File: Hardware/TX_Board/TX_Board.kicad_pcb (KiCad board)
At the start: 2 copper layers, 153 x 131.5 mm, 218 parts, among them IC1 QPA9122TR7, IC10 QPA9122TR7, IC11 QPA9122TR7, IC12 LT3041ADE#PBF, IC13 LT3099ADE#PBF, IC14 ADPL40502AUJZ-1.5-R7, IC2 MAPS-010164-TR0500, IC3 MAPS-010164-TR0500, IC4 QPA9122TR7, IC5 GP2Y1+, IC6 GP2Y1+, IC7 GP2Y1+, IC8 MAPS-010164-TR0500, IC9 MAPS-010164-TR0500, J1 Conn_Coaxial, J10 Conn_01x01_Pin, J11 Conn_Coaxial, J12 Conn_02x04_Odd_Even, J13 MM8030-2610RJ3, J14 MM8030-2610RJ3, J15 MM8030-2610RJ3, J16 MM8030-2610RJ3, J17 MM8030-2610RJ3, J18 MM8030-2610RJ3, J19 MM8030-2610RJ3, J2 Conn_Coaxial, J20 MM8030-2610RJ3, J21 MM8030-2610RJ3, J22 MM8030-2610RJ3, J23 MM8030-2610RJ3, J24 MM8030-2610RJ3, J3 Conn_Coaxial, J4 Conn_Coaxial, J5 Conn_02x08_Odd_Even, J6 Conn_01x03_Socket, J7 Conn_01x01_Pin, J8 Conn_01x01_Pin, J9 Conn_01x01_Pin, U1 SN74HCT138NSR, U2 LDO40LPU50RY, U3 ADP7182AUJZ-5.0

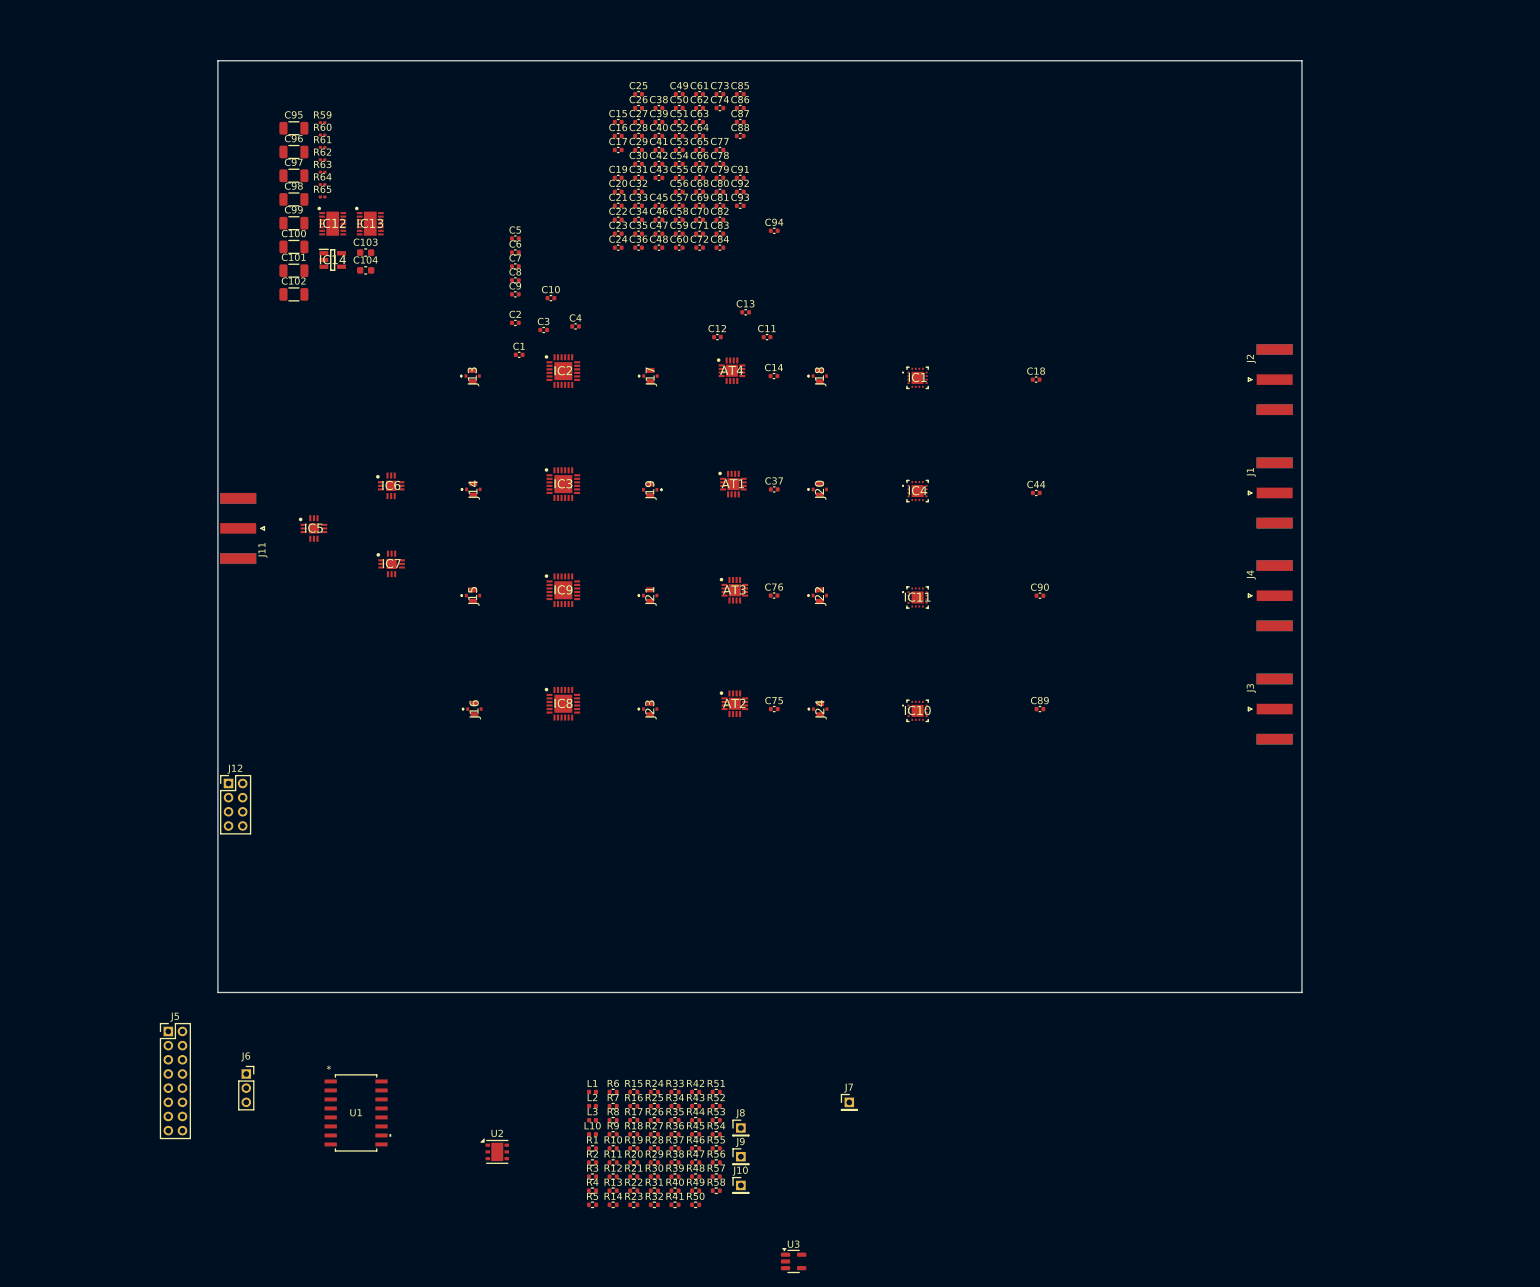
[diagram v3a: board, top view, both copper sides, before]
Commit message: updated schematics
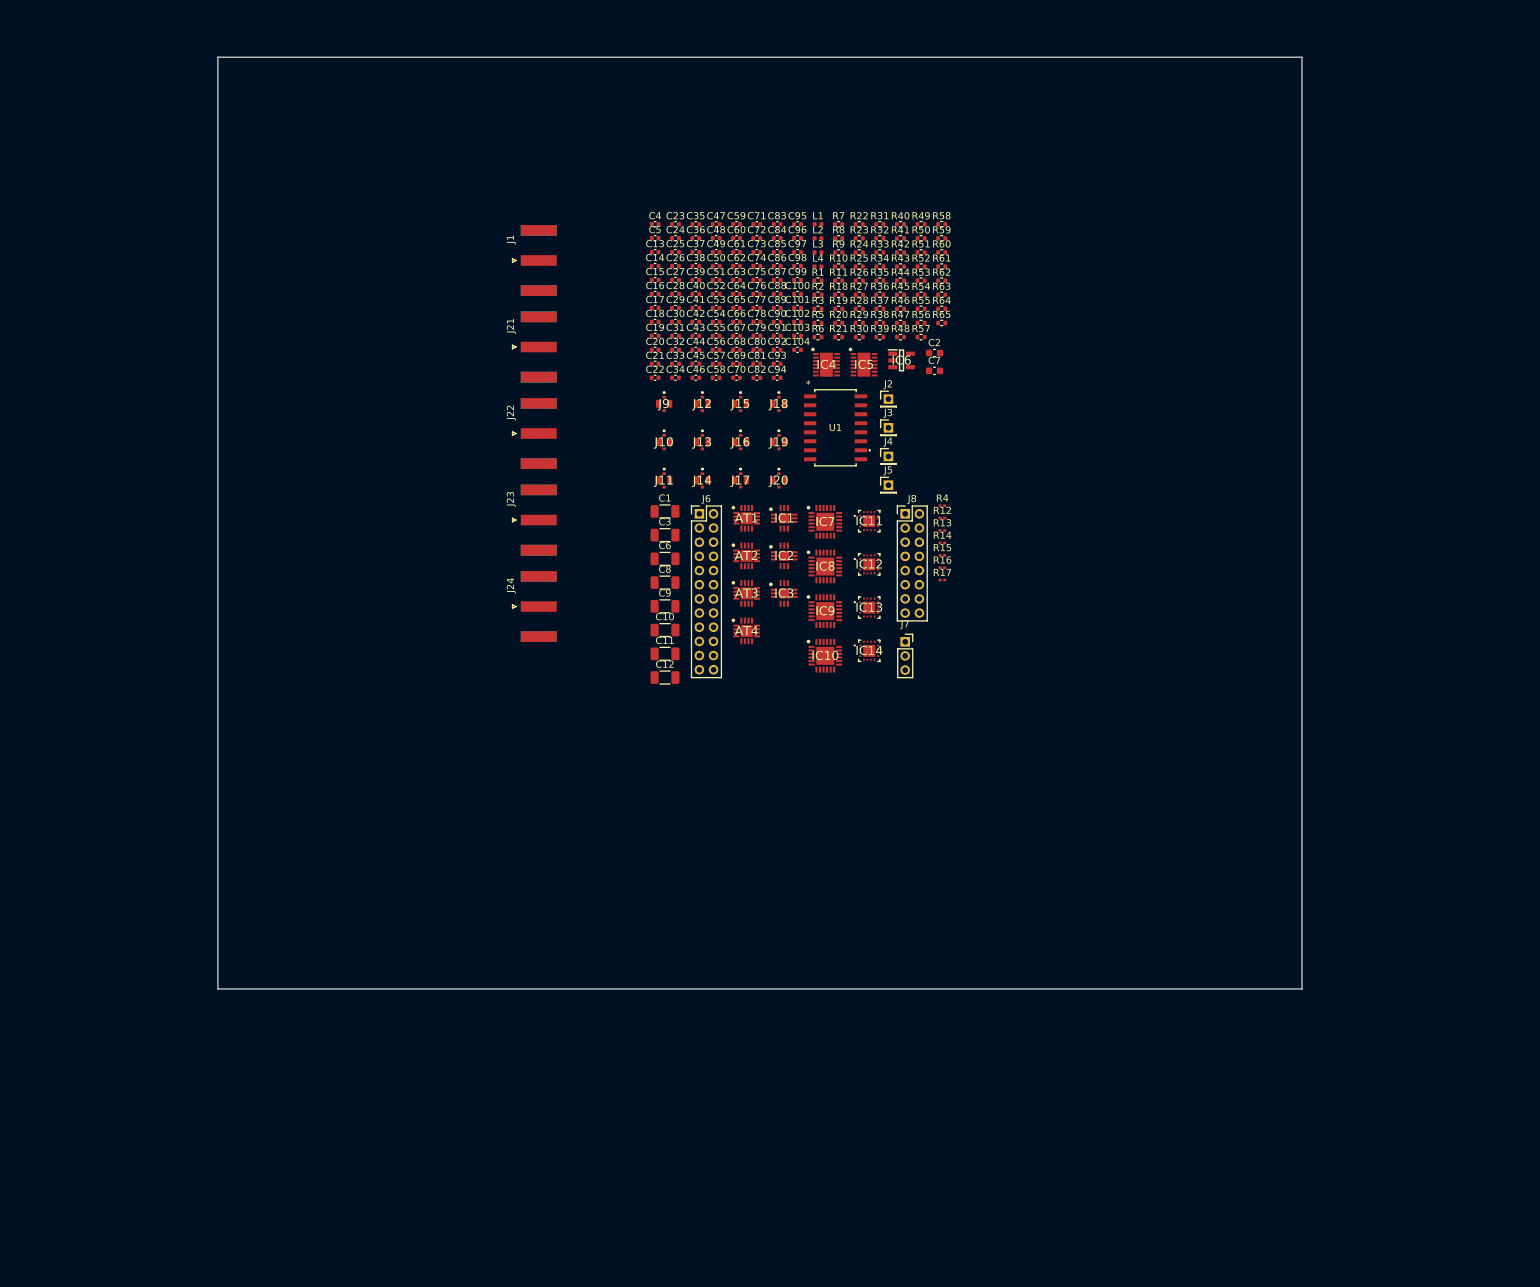
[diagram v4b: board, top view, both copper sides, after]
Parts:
- removed L10: 12 nH, Inductor_SMD:L_0402_1005Metric
- removed U2: LDO40LPU50RY, Package_DFN_QFN:DFN-6-1EP_3x3mm_P0.95mm_EP1.7x2.6mm
- removed U3: ADP7182AUJZ-5.0, Package_TO_SOT_SMD:TSOT-23-5
- added L4: 12 nH, Inductor_SMD:L_0402_1005Metric, F.Cu at (139.2, 55.0)
- C1, C3, C9: value 0.1uF -> 10uF; footprint Capacitor_SMD:C_0402_1005Metric -> Capacitor_SMD:C_1206_3216Metric
- C10, C6: value 300pF -> 10uF; footprint Capacitor_SMD:C_0402_1005Metric -> Capacitor_SMD:C_1206_3216Metric
- C100, C97: value 10uF -> 1 uF; footprint Capacitor_SMD:C_1206_3216Metric -> Capacitor_SMD:C_0402_1005Metric
- C101, C96, C98: value 10uF -> 100 pF; footprint Capacitor_SMD:C_1206_3216Metric -> Capacitor_SMD:C_0402_1005Metric
- C102: value 4.7uF -> 18 pF; footprint Capacitor_SMD:C_1206_3216Metric -> Capacitor_SMD:C_0402_1005Metric
- C103, C104: value 1uF -> 18 pF; footprint Capacitor_SMD:C_0603_1608Metric -> Capacitor_SMD:C_0402_1005Metric
- C11: value 470p -> 4.7uF; footprint Capacitor_SMD:C_0402_1005Metric -> Capacitor_SMD:C_1206_3216Metric
- C12: value 1uF -> 4.7uF; footprint Capacitor_SMD:C_0402_1005Metric -> Capacitor_SMD:C_1206_3216Metric
- C13, C19: value 300pF -> 0.1uF
- C14: value 18 pF -> 0.1uF
- C15, C17, C41, C43: value 100 pF -> 0.1uF
- C16: value 1 uF -> 0.1uF
- C18, C44: value 18 pF -> 100pF
- C2: value 100pF -> 1uF; footprint Capacitor_SMD:C_0402_1005Metric -> Capacitor_SMD:C_0603_1608Metric
- C20, C26, C27, C28, C5: value 300pF -> 100pF
- C22: value 100 pF -> 100pF
- C29, C49, C61: value 0.1uF -> 300pF
- C30, C50, C51, C52, C62: value 100pF -> 300pF
- C32, C65, C67: value 470p -> 300pF
- C33, C66, C68: value 1uF -> 300pF
- C37: value 18 pF -> 300pF
- C38, C40: value 100 pF -> 300pF
- C39: value 1 uF -> 300pF
- C4: value 100pF -> 0.1uF
- C42: value 1 uF -> 100pF
- C46: value 0.1uF -> 100pF
- C53, C55, C57: value 300pF -> 470p
- C54, C56, C58: value 300pF -> 1uF
- C59: value 0.1uF -> 470p
- C60: value 100pF -> 1uF
- C7: value 300pF -> 1uF; footprint Capacitor_SMD:C_0402_1005Metric -> Capacitor_SMD:C_0603_1608Metric
- C72, C74: value 300pF -> 18 pF
- C8: value 100pF -> 10uF; footprint Capacitor_SMD:C_0402_1005Metric -> Capacitor_SMD:C_1206_3216Metric
- C82, C84: value 100 pF -> 1 uF
- C85, C87: value 1 uF -> 100 pF
- C89, C90: value 18 pF -> 100 pF
- C91: value 0.1uF -> 100 pF
- C92: value 100pF -> 100 pF
- C95: value 4.7uF -> 1 uF; footprint Capacitor_SMD:C_1206_3216Metric -> Capacitor_SMD:C_0402_1005Metric
- C99: value 10uF -> 18 pF; footprint Capacitor_SMD:C_1206_3216Metric -> Capacitor_SMD:C_0402_1005Metric
- IC1: value QPA9122TR7 -> GP2Y1+; footprint QPA9122TR7:QPA9122TR7 -> GP2Y1+:QFN51P300X300X89-13N
- IC10: value QPA9122TR7 -> MAPS-010164-TR0500; footprint QPA9122TR7:QPA9122TR7 -> MAPS-010164-TR0500:QFN50P400X400X100-25N-D
- IC12: value LT3041ADE#PBF -> QPA9122TR7; footprint LT3041ADE:SON50P300X400X80-15N-D -> QPA9122TR7:QPA9122TR7
- IC13: value LT3099ADE#PBF -> QPA9122TR7; footprint LT3099ADE:SON50P300X400X80-15N-D -> QPA9122TR7:QPA9122TR7
- IC14: value ADPL40502AUJZ-1.5-R7 -> QPA9122TR7; footprint ADPL40502:SOT95P280X100-5N -> QPA9122TR7:QPA9122TR7
- IC2, IC3: value MAPS-010164-TR0500 -> GP2Y1+; footprint MAPS-010164-TR0500:QFN50P400X400X100-25N-D -> GP2Y1+:QFN51P300X300X89-13N
- IC4: value QPA9122TR7 -> LT3041ADE#PBF; footprint QPA9122TR7:QPA9122TR7 -> LT3041ADE:SON50P300X400X80-15N-D
- IC5: value GP2Y1+ -> LT3099ADE#PBF; footprint GP2Y1+:QFN51P300X300X89-13N -> LT3099ADE:SON50P300X400X80-15N-D
- IC6: value GP2Y1+ -> ADPL40502AUJZ-1.5-R7; footprint GP2Y1+:QFN51P300X300X89-13N -> ADPL40502:SOT95P280X100-5N
- IC7: value GP2Y1+ -> MAPS-010164-TR0500; footprint GP2Y1+:QFN51P300X300X89-13N -> MAPS-010164-TR0500:QFN50P400X400X100-25N-D
- J10, J9: value Conn_01x01_Pin -> MM8030-2610RJ3; footprint Connector_PinHeader_2.00mm:PinHeader_1x01_P2.00mm_Vertical -> MM8030:MM80302610RJ3
- J11: value Conn_Coaxial -> MM8030-2610RJ3; footprint Connector_Coaxial:SMA_Amphenol_132289_EdgeMount -> MM8030:MM80302610RJ3
- J12: value Conn_02x04_Odd_Even -> MM8030-2610RJ3; footprint Connector_PinHeader_2.00mm:PinHeader_2x04_P2.00mm_Vertical -> MM8030:MM80302610RJ3
- J2, J3, J4: value Conn_Coaxial -> Conn_01x01_Pin; footprint Connector_Coaxial:SMA_Amphenol_132289_EdgeMount -> Connector_PinHeader_2.00mm:PinHeader_1x01_P2.00mm_Vertical
- J21, J22, J23, J24: value MM8030-2610RJ3 -> Conn_Coaxial; footprint MM8030:MM80302610RJ3 -> Connector_Coaxial:SMA_Amphenol_132289_EdgeMount
- J5: value Conn_02x08_Odd_Even -> Conn_01x01_Pin; footprint Connector_PinHeader_2.00mm:PinHeader_2x08_P2.00mm_Vertical -> Connector_PinHeader_2.00mm:PinHeader_1x01_P2.00mm_Vertical
- J6: value Conn_01x03_Socket -> Conn_02x12_Odd_Even; footprint Connector_PinSocket_2.00mm:PinSocket_1x03_P2.00mm_Vertical -> Connector_PinHeader_2.00mm:PinHeader_2x12_P2.00mm_Vertical
- J7: value Conn_01x01_Pin -> Conn_01x03_Socket; footprint Connector_PinHeader_2.00mm:PinHeader_1x01_P2.00mm_Vertical -> Connector_PinSocket_2.00mm:PinSocket_1x03_P2.00mm_Vertical
- J8: value Conn_01x01_Pin -> Conn_02x08_Odd_Even; footprint Connector_PinHeader_2.00mm:PinHeader_1x01_P2.00mm_Vertical -> Connector_PinHeader_2.00mm:PinHeader_2x08_P2.00mm_Vertical
- R1, R2: value 10 -> 1M
- R10, R11, R3, R5: value 10 -> 0
- R12, R14: value 10 -> 453k; footprint Resistor_SMD:R_0402_1005Metric -> Resistor_SMD:R_0201_0603Metric
- R13, R15, R16, R17: value 10 -> 49.9k; footprint Resistor_SMD:R_0402_1005Metric -> Resistor_SMD:R_0201_0603Metric
- R19, R38, R39: value 8.2 -> 10
- R20, R22, R23, R40, R41, R44, R45: value 0 -> 10
- R21, R42, R43: value 51 -> 10
- R4: value 10 -> 200k; footprint Resistor_SMD:R_0402_1005Metric -> Resistor_SMD:R_0201_0603Metric
- R46, R47, R48, R49: value 0 -> 8.2
- R54, R55: value 0 -> 51
- R56, R57: value 1M -> 51
- R59, R60, R63, R65: value 49.9k -> 0; footprint Resistor_SMD:R_0201_0603Metric -> Resistor_SMD:R_0402_1005Metric
- R6: value 51 -> 0
- R61, R64: value 453k -> 0; footprint Resistor_SMD:R_0201_0603Metric -> Resistor_SMD:R_0402_1005Metric
- R62: value 200k -> 0; footprint Resistor_SMD:R_0201_0603Metric -> Resistor_SMD:R_0402_1005Metric
- R9: value 8.2 -> 0
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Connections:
- AT3 pad 15: ATTN_A1_1 -> ATTN_A1
- AT3 pad 16: ATTN_A2_1 -> ATTN_A2
- AT3 pad 2: ATTN_A0_1 -> ATTN_A0
- AT4 pad 15: ATTN_A1_1 -> ATTN_A1
- AT4 pad 16: ATTN_A2_1 -> ATTN_A2
- AT4 pad 2: ATTN_A0_1 -> ATTN_A0
- C1 pad 1: VCC -> GND
- C1 pad 2: GND -> +VDC
- C10 pad 1: Net-(IC2-SER_OUT) -> GND
- C10 pad 2: GND -> VEE
- C100 pad 1: GND -> Net-(C100-Pad1)
- C100 pad 2: VEE -> GND
- C101 pad 1: GND -> Net-(C100-Pad1)
- C101 pad 2: VEE -> GND
- C102 pad 1: Net-(IC13-SET) -> Net-(IC12-RFOUT/VCC3_1)
- C102 pad 2: GND -> Net-(J22-In)
- C103 pad 1: V_PD -> Net-(IC13-RFOUT/VCC3_1)
- C103 pad 2: GND -> Net-(J23-In)
- C104 pad 1: GND -> Net-(IC14-RFOUT/VCC3_1)
- C104 pad 2: VCC -> Net-(J24-In)
- C11 pad 1: VCC -> Net-(IC4-SET)
- C12 pad 1: VCC -> Net-(IC5-SET)
- C13 pad 1: Net-(AT4-SI) -> VCC
- C14 pad 1: Net-(AT4-RFOUT) -> VCC
- C14 pad 2: Net-(J18-IN) -> GND
- C17 pad 2: Net-(C17-Pad2) -> VEE
- C18 pad 1: Net-(IC1-RFOUT/VCC3_1) -> VCC
- C18 pad 2: Net-(J2-In) -> GND
- C19 pad 1: Net-(AT4-CLK) -> GND
- C19 pad 2: GND -> VEE
- C2 pad 1: VCC -> GND
- C2 pad 2: GND -> VCC
- C20 pad 1: GND -> VCC
- C20 pad 2: Net-(AT4-LE) -> GND
- C21 pad 1: VCC -> GND
- C21 pad 2: GND -> VEE
- C22 pad 1: Net-(C17-Pad2) -> VCC
- C26 pad 1: Net-(IC3-D1_OR_SER_IN) -> GND
- C26 pad 2: GND -> VEE
- C27 pad 2: Net-(IC3-D2_OR_CLK) -> VEE
- C28 pad 2: Net-(IC3-D3_OR_LE) -> VEE
- C29 pad 1: VCC -> Net-(IC7-D1_OR_SER_IN)
- C3 pad 2: VEE -> -VDC
- C30 pad 1: GND -> Net-(IC8-D1_OR_SER_IN)
- C30 pad 2: VCC -> GND
- C31 pad 1: Net-(IC3-SER_OUT) -> Net-(IC9-D1_OR_SER_IN)
- C32 pad 1: VCC -> Net-(IC10-D1_OR_SER_IN)
- C33 pad 1: VCC -> GND
- C33 pad 2: GND -> Net-(IC7-D2_OR_CLK)
- C34 pad 1: Net-(AT1-SI) -> GND
- C34 pad 2: GND -> Net-(IC8-D2_OR_CLK)
- C35 pad 1: Net-(AT1-CLK) -> GND
- C35 pad 2: GND -> Net-(IC9-D2_OR_CLK)
- C36 pad 2: Net-(AT1-LE) -> Net-(IC7-D3_OR_LE)
- C37 pad 1: Net-(AT1-RFOUT) -> GND
- C37 pad 2: Net-(J20-IN) -> Net-(IC10-D2_OR_CLK)
- C38 pad 1: VCC -> GND
- C38 pad 2: GND -> Net-(IC8-D3_OR_LE)
- C39 pad 1: VCC -> GND
- C39 pad 2: GND -> Net-(IC9-D3_OR_LE)
- C4 pad 2: VEE -> VCC
- C40 pad 2: Net-(C40-Pad2) -> Net-(IC10-D3_OR_LE)
- C41 pad 1: Net-(C40-Pad2) -> VCC
- C42 pad 1: Net-(C42-Pad1) -> GND
- C42 pad 2: GND -> VCC
- C43 pad 1: Net-(C42-Pad1) -> VCC
- C44 pad 1: Net-(IC4-RFOUT/VCC3_1) -> GND
- C44 pad 2: Net-(J1-In) -> VCC
- C46 pad 1: VCC -> GND
- C46 pad 2: GND -> VCC
- C47 pad 1: GND -> VCC
- C47 pad 2: VEE -> GND
- C48 pad 1: VCC -> GND
- C48 pad 2: GND -> VCC
- C49 pad 1: GND -> Net-(IC7-SER_OUT)
- C49 pad 2: VEE -> GND
- C5 pad 1: Net-(IC2-D1_OR_SER_IN) -> GND
- C5 pad 2: GND -> VCC
- C50 pad 1: VCC -> Net-(IC8-SER_OUT)
- C51 pad 1: GND -> Net-(IC9-SER_OUT)
- C51 pad 2: VEE -> GND
- C52 pad 1: GND -> Net-(IC10-SER_OUT)
- C52 pad 2: VEE -> GND
- C53 pad 1: Net-(IC8-D1_OR_SER_IN) -> VCC
- C54 pad 1: Net-(IC9-D1_OR_SER_IN) -> VCC
- C55 pad 1: GND -> VCC
- C55 pad 2: Net-(IC8-D2_OR_CLK) -> GND
- C56 pad 1: GND -> VCC
- C56 pad 2: Net-(IC9-D2_OR_CLK) -> GND
- C57 pad 1: GND -> VCC
- C57 pad 2: Net-(IC8-D3_OR_LE) -> GND
- C58 pad 1: GND -> VCC
- C58 pad 2: Net-(IC9-D3_OR_LE) -> GND
- C6 pad 2: Net-(IC2-D3_OR_LE) -> VCC
- C60 pad 1: GND -> VCC
- C60 pad 2: VCC -> GND
- C61 pad 1: VCC -> Net-(AT1-SI)
- C62 pad 1: GND -> Net-(AT2-SI)
- C62 pad 2: VCC -> GND
- C63 pad 1: Net-(IC8-SER_OUT) -> Net-(AT3-SI)
- C64 pad 1: Net-(IC9-SER_OUT) -> Net-(AT4-SI)
- C65 pad 1: VCC -> Net-(AT1-CLK)
- C66 pad 1: VCC -> Net-(AT2-CLK)
- C67 pad 1: VCC -> Net-(AT3-CLK)
- C68 pad 1: VCC -> Net-(AT4-CLK)
- C69 pad 1: Net-(AT2-SI) -> GND
- C69 pad 2: GND -> Net-(AT1-LE)
- C7 pad 1: GND -> V_PD
- C7 pad 2: Net-(IC2-D2_OR_CLK) -> GND
- C70 pad 1: Net-(AT3-SI) -> GND
- C70 pad 2: GND -> Net-(AT2-LE)
- C71 pad 1: Net-(AT2-CLK) -> GND
- C71 pad 2: GND -> Net-(AT3-LE)
- C72 pad 1: Net-(AT3-CLK) -> Net-(AT1-RFOUT)
- C72 pad 2: GND -> Net-(J17-IN)
- C73 pad 2: Net-(AT2-LE) -> Net-(AT4-LE)
- C74 pad 1: GND -> Net-(AT2-RFOUT)
- C74 pad 2: Net-(AT3-LE) -> Net-(J18-IN)
- C75 pad 1: Net-(AT2-RFOUT) -> Net-(AT3-RFOUT)
- C75 pad 2: Net-(J24-IN) -> Net-(J19-IN)
- C76 pad 1: Net-(AT3-RFOUT) -> Net-(AT4-RFOUT)
- C76 pad 2: Net-(J22-IN) -> Net-(J20-IN)
- C81 pad 1: GND -> VCC
- C81 pad 2: Net-(C81-Pad2) -> GND
- C82 pad 1: GND -> VCC
- C82 pad 2: Net-(C82-Pad2) -> GND
- C83 pad 1: Net-(C81-Pad2) -> VCC
- C84 pad 1: Net-(C82-Pad2) -> VCC
- C85 pad 1: Net-(C85-Pad1) -> GND
- C85 pad 2: GND -> Net-(C85-Pad2)
- C86 pad 1: Net-(C85-Pad1) -> GND
- C86 pad 2: GND -> Net-(C86-Pad2)
- C87 pad 1: Net-(C87-Pad1) -> GND
- C87 pad 2: GND -> Net-(C87-Pad2)
- C88 pad 1: Net-(C87-Pad1) -> GND
- C88 pad 2: GND -> Net-(C88-Pad2)
- C89 pad 1: Net-(IC10-RFOUT/VCC3_1) -> Net-(C85-Pad2)
- C89 pad 2: Net-(J3-In) -> GND
- C9 pad 1: VCC -> GND
- C9 pad 2: GND -> VEE
- C90 pad 1: Net-(IC11-RFOUT/VCC3_1) -> Net-(C86-Pad2)
- C90 pad 2: Net-(J4-In) -> GND
- C91 pad 1: GND -> Net-(C87-Pad2)
- C91 pad 2: VCC -> GND
- C92 pad 1: GND -> Net-(C88-Pad2)
- C92 pad 2: VCC -> GND
- C95 pad 1: Net-(IC12-SET) -> Net-(C95-Pad1)
- C96 pad 1: GND -> Net-(C95-Pad1)
- C96 pad 2: +VDC -> GND
- C97 pad 1: GND -> Net-(C97-Pad1)
- C97 pad 2: VCC -> GND
- C98 pad 1: GND -> Net-(C97-Pad1)
- C98 pad 2: VCC -> GND
- C99 pad 1: GND -> Net-(IC11-RFOUT/VCC3_1)
- C99 pad 2: -VDC -> Net-(J21-In)
- IC1 pad 10: Net-(IC1-RFOUT/VCC3_1) -> GND
- IC1 pad 11: Net-(IC1-RFOUT/VCC3_1) -> GND
- IC1 pad 13: Net-(IC1-VBIAS) -> GND
- IC1 pad 2: Net-(IC1-RFIN) -> Net-(IC1-SUM_PORT)
- IC1 pad 4: Net-(IC1-VCC1/VCC2) -> GND
- IC1 pad 7: GND -> Net-(IC1-PORT_1)
- IC1 pad 9: GND -> Net-(IC1-PORT_2)
- IC10 pad 1: GND -> VEE
- IC10 pad 10: Net-(IC10-RFOUT/VCC3_1) -> GND
- IC10 pad 11: Net-(IC10-RFOUT/VCC3_1) -> GND
- IC10 pad 13: Net-(IC10-VBIAS) -> GND
- IC10 pad 14: GND -> Net-(IC10-RF_OUT)
- IC10 pad 16: Net-(IC10-VPD) -> GND
- IC10 pad 17: GND -> Net-(IC10-SER_OUT)
- IC10 pad 2: Net-(IC10-RFIN) -> VCC
- IC10 pad 4: Net-(IC10-VCC1/VCC2) -> GND
- IC10 pad 5: GND -> RF_IN1
- IC12 pad 1: +VDC -> GND
- IC12 pad 10: GND -> Net-(IC12-RFOUT/VCC3_1)
- IC12 pad 11: GND -> Net-(IC12-RFOUT/VCC3_1)
- IC12 pad 12: VCC -> GND
- IC12 pad 13: VCC -> Net-(IC12-VBIAS)
- IC12 pad 14: VCC -> GND
- IC12 pad 2: +VDC -> Net-(IC12-RFIN)
- IC12 pad 3: +VDC -> GND
- IC12 pad 4: unconnected-(IC12-VIOC-Pad4) -> Net-(IC12-VCC1/VCC2)
- IC12 pad 5: +VDC -> GND
- IC12 pad 6: Net-(IC12-PG) -> GND
- IC12 pad 8: Net-(IC12-PGFB) -> GND
- IC12 pad 9: Net-(IC12-SET) -> GND
- IC13 pad 1: -VDC -> GND
- IC13 pad 10: GND -> Net-(IC13-RFOUT/VCC3_1)
- IC13 pad 11: GND -> Net-(IC13-RFOUT/VCC3_1)
- IC13 pad 12: VEE -> GND
- IC13 pad 13: VEE -> Net-(IC13-VBIAS)
- IC13 pad 14: VEE -> GND
- IC13 pad 15: -VDC -> GND
- IC13 pad 2: -VDC -> Net-(IC13-RFIN)
- IC13 pad 3: -VDC -> GND
- IC13 pad 4: -VDC -> Net-(IC13-VCC1/VCC2)
- IC13 pad 5: unconnected-(IC13-PG-Pad5) -> GND
- IC13 pad 6: unconnected-(IC13-VIOC-Pad6) -> GND
- IC13 pad 8: Net-(IC13-PGFB) -> GND
- IC13 pad 9: Net-(IC13-SET) -> GND
- IC14 pad 1: VCC -> GND
- IC14 pad 2: GND -> Net-(IC14-RFIN)
- IC14 pad 3: VCC -> GND
- IC14 pad 4: unconnected-(IC14-NC-Pad4) -> Net-(IC14-VCC1/VCC2)
- IC14 pad 5: V_PD -> GND
- IC2 pad 1: VEE -> GND
- IC2 pad 2: VCC -> Net-(IC1-PORT_1)
- IC2 pad 5: RF_IN1 -> GND
- IC2 pad 7: GND -> Net-(IC2-PORT_1)
- IC2 pad 9: GND -> Net-(IC2-PORT_2)
- IC3 pad 1: VEE -> GND
- IC3 pad 2: VCC -> Net-(IC1-PORT_2)
- IC3 pad 5: RF_IN2 -> GND
- IC3 pad 7: GND -> Net-(IC3-PORT_1)
- IC3 pad 9: GND -> Net-(IC3-PORT_2)
- IC4 pad 1: GND -> +VDC
- IC4 pad 10: Net-(IC4-RFOUT/VCC3_1) -> GND
- IC4 pad 11: Net-(IC4-RFOUT/VCC3_1) -> GND
- IC4 pad 12: GND -> VCC
- IC4 pad 13: Net-(IC4-VBIAS) -> VCC
- IC4 pad 14: GND -> VCC
- IC4 pad 2: Net-(IC4-RFIN) -> +VDC
- IC4 pad 3: GND -> +VDC
- IC4 pad 4: Net-(IC4-VCC1/VCC2) -> unconnected-(IC4-VIOC-Pad4)
- IC4 pad 5: GND -> +VDC
- IC4 pad 6: GND -> Net-(IC4-PG)
- IC4 pad 8: GND -> Net-(IC4-PGFB)
- IC4 pad 9: GND -> Net-(IC4-SET)
- IC5 pad 1: GND -> -VDC
- IC5 pad 12: GND -> VEE
- IC5 pad 13: GND -> VEE
- IC5 pad 2: Net-(IC5-SUM_PORT) -> -VDC
- IC5 pad 3: GND -> -VDC
- IC5 pad 4: GND -> -VDC
- IC5 pad 5: GND -> unconnected-(IC5-PG-Pad5)
- IC5 pad 6: GND -> unconnected-(IC5-VIOC-Pad6)
- IC5 pad 7: Net-(IC5-PORT_1) -> GND
- IC5 pad 8: GND -> Net-(IC5-PGFB)
- IC5 pad 9: Net-(IC5-PORT_2) -> Net-(IC5-SET)
- IC6 pad 1: GND -> VCC
- IC6 pad 2: Net-(IC5-PORT_2) -> GND
- IC6 pad 3: GND -> VCC
- IC6 pad 4: GND -> unconnected-(IC6-NC-Pad4)
- IC6 pad 5: GND -> V_PD
- IC7 pad 1: GND -> VEE
- IC7 pad 2: Net-(IC5-PORT_1) -> VCC
- IC7 pad 5: GND -> RF_IN4
- IC7 pad 7: Net-(IC7-PORT_1) -> GND
- IC7 pad 9: Net-(IC7-PORT_2) -> GND
- IC8 pad 5: RF_IN4 -> RF_IN2
- J1 pad 1: Net-(J1-In) -> Net-(IC1-SUM_PORT)
- J10 pad 1: unconnected-(J10-Pin_1-Pad1) -> Net-(IC3-PORT_1)
- J11 pad 1: Net-(IC5-SUM_PORT) -> Net-(IC2-PORT_2)
- J11 pad 2: GND -> RF_IN3
- J12 pad 1: GPIO0 -> Net-(IC2-PORT_1)
- J12 pad 2: GPIO0 -> RF_IN4
- J12 pad 3: GPIO1 -> GND
- J12 pad 4: GPIO1 -> GND
- J13 pad 1: Net-(IC6-PORT_2) -> Net-(IC8-RF_OUT)
- J13 pad 2: RF_IN1 -> Net-(AT2-RFIN)
- J14 pad 1: Net-(IC6-PORT_1) -> Net-(IC9-RF_OUT)
- J14 pad 2: RF_IN2 -> Net-(AT3-RFIN)
- J15 pad 1: Net-(IC7-PORT_2) -> Net-(IC7-RF_OUT)
- J15 pad 2: RF_IN3 -> Net-(AT1-RFIN)
- J16 pad 1: Net-(IC7-PORT_1) -> Net-(IC10-RF_OUT)
- J16 pad 2: RF_IN4 -> Net-(AT4-RFIN)
- J17 pad 1: Net-(IC2-RF_OUT) -> Net-(J17-IN)
- J17 pad 2: Net-(AT4-RFIN) -> Net-(IC11-RFIN)
- J18 pad 2: Net-(IC1-RFIN) -> Net-(IC12-RFIN)
- J19 pad 1: Net-(IC3-RF_OUT) -> Net-(J19-IN)
- J19 pad 2: Net-(AT1-RFIN) -> Net-(IC13-RFIN)
- J2 pad 1: Net-(J2-In) -> unconnected-(J2-Pin_1-Pad1)
- J20 pad 2: Net-(IC4-RFIN) -> Net-(IC14-RFIN)
- J21 pad 1: Net-(IC9-RF_OUT) -> Net-(J21-In)
- J21 pad 2: Net-(AT3-RFIN) -> GND
- J22 pad 1: Net-(J22-IN) -> Net-(J22-In)
- J22 pad 2: Net-(IC11-RFIN) -> GND
- J23 pad 1: Net-(IC8-RF_OUT) -> Net-(J23-In)
- J23 pad 2: Net-(AT2-RFIN) -> GND
- J24 pad 1: Net-(J24-IN) -> Net-(J24-In)
- J24 pad 2: Net-(IC10-RFIN) -> GND
- J3 pad 1: Net-(J3-In) -> unconnected-(J3-Pin_1-Pad1)
- J4 pad 1: Net-(J4-In) -> unconnected-(J4-Pin_1-Pad1)
- J5 pad 1: PS_LE_1 -> unconnected-(J5-Pin_1-Pad1)
- J6 pad 1: +VDC -> GPIO0
- J6 pad 2: GND -> GPIO0
- J6 pad 3: -VDC -> GPIO1
- J7 pad 1: unconnected-(J7-Pin_1-Pad1) -> +VDC
- J8 pad 1: unconnected-(J8-Pin_1-Pad1) -> PS_LE_1
- J9 pad 1: unconnected-(J9-Pin_1-Pad1) -> Net-(IC3-PORT_2)
- L1 pad 1: Net-(IC4-RFOUT/VCC3_1) -> Net-(IC11-RFOUT/VCC3_1)
- L1 pad 2: Net-(C42-Pad1) -> Net-(C93-Pad1)
- L2 pad 1: Net-(IC10-RFOUT/VCC3_1) -> Net-(IC12-RFOUT/VCC3_1)
- L2 pad 2: Net-(C85-Pad1) -> Net-(C95-Pad1)
- L3 pad 1: Net-(IC11-RFOUT/VCC3_1) -> Net-(IC13-RFOUT/VCC3_1)
- L3 pad 2: Net-(C87-Pad1) -> Net-(C97-Pad1)
- R1 pad 1: PS_SER_IN -> GND
- R1 pad 2: Net-(IC2-D1_OR_SER_IN) -> Net-(U1-*G2A)
- R10 pad 1: Net-(AT4-CLK) -> Net-(U1-Y5)
- R10 pad 2: ATTN_CLK -> ATTN_LE_3
- R11 pad 1: Net-(AT4-LE) -> Net-(U1-Y6)
- R11 pad 2: ATTN_LE_1 -> PS_LE_4
- R12 pad 1: PS_SER_IN -> VCC
- R12 pad 2: Net-(IC3-D1_OR_SER_IN) -> Net-(IC4-PGFB)
- R13 pad 1: PS_CLK -> Net-(IC4-PGFB)
- R13 pad 2: Net-(IC3-D2_OR_CLK) -> GND
- R14 pad 1: Net-(IC3-D3_OR_LE) -> VEE
- R14 pad 2: PS_LE_2 -> Net-(IC5-PGFB)
- R15 pad 1: SER OUT -> Net-(IC5-PGFB)
- R15 pad 2: Net-(IC3-SER_OUT) -> GND
- R16 pad 1: ATTN_SI -> GND
- R16 pad 2: Net-(AT1-SI) -> Net-(IC4-SET)
- R17 pad 1: Net-(AT1-CLK) -> GND
- R17 pad 2: ATTN_CLK -> Net-(IC5-SET)
- R18 pad 1: Net-(AT1-LE) -> PS_SER_IN
- R18 pad 2: ATTN_LE_2 -> Net-(IC7-D1_OR_SER_IN)
- R19 pad 1: VCC -> PS_SER_IN
- R19 pad 2: Net-(IC4-VCC1/VCC2) -> Net-(IC8-D1_OR_SER_IN)
- R2 pad 1: PS_CLK -> GND
- R2 pad 2: Net-(IC2-D2_OR_CLK) -> Net-(U1-*G2B)
- R20 pad 1: V_PD -> PS_SER_IN
- R20 pad 2: Net-(IC4-VPD) -> Net-(IC9-D1_OR_SER_IN)
- R21 pad 1: Net-(C40-Pad2) -> PS_SER_IN
- R21 pad 2: Net-(IC4-VBIAS) -> Net-(IC10-D1_OR_SER_IN)
- R22 pad 1: Net-(C40-Pad2) -> PS_CLK
- R22 pad 2: VCC -> Net-(IC7-D2_OR_CLK)
- R23 pad 1: Net-(C42-Pad1) -> PS_CLK
- R23 pad 2: VCC -> Net-(IC8-D2_OR_CLK)
- R24 pad 1: PS_SER_IN -> PS_CLK
- R24 pad 2: Net-(IC8-D1_OR_SER_IN) -> Net-(IC9-D2_OR_CLK)
- R25 pad 1: PS_SER_IN -> Net-(IC7-D3_OR_LE)
- R25 pad 2: Net-(IC9-D1_OR_SER_IN) -> PS_LE_4
- R26 pad 2: Net-(IC8-D2_OR_CLK) -> Net-(IC10-D2_OR_CLK)
- R27 pad 1: PS_CLK -> Net-(IC8-D3_OR_LE)
- R27 pad 2: Net-(IC9-D2_OR_CLK) -> PS_LE_2
- R28 pad 1: Net-(IC8-D3_OR_LE) -> Net-(IC9-D3_OR_LE)
- R28 pad 2: PS_LE_4 -> PS_LE_3
- R29 pad 1: Net-(IC9-D3_OR_LE) -> Net-(IC10-D3_OR_LE)
- R29 pad 2: PS_LE_3 -> PS_LE_1
- R3 pad 1: Net-(IC2-D3_OR_LE) -> ATTN_LE_4
- R3 pad 2: PS_LE_1 -> Net-(U1-Y7)
- R30 pad 1: SER OUT -> PS_SER_OUT
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
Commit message: refactored pcb
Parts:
- AT1, AT2, AT3, AT4: footprint RFSA3713TR7:QFN50P300X300X90-17N -> tx_board_footprints:QFN50P300X300X90-17N
- C100, C78, C80: value 1 uF -> 100 pF
- C102, C76, C99: value 18 pF -> 1 uF
- C103, C75: value 18 pF -> 100 pF
- C15, C16, C21: value 0.1uF -> 100pF
- C17, C19, C41, C45: value 0.1uF -> 300pF
- C18, C22, C25, C26, C27, C42, C48: value 100pF -> 300pF
- C20: value 100pF -> 0.1uF
- C23: value 0.1uF -> 470p
- C24: value 100pF -> 1uF
- C28: value 100pF -> 18 pF
- C29, C31, C32, C34, C52: value 300pF -> 100 pF
- C30, C33: value 300pF -> 1 uF
- C35, C51: value 300pF -> 18 pF
- C36, C37, C66: value 300pF -> 0.1uF
- C38, C39, C61, C62, C67: value 300pF -> 100pF
- C46: value 100pF -> 470p
- C47: value 0.1uF -> 1uF
- C53: value 470p -> 1 uF
- C54: value 1uF -> 100 pF
- C55, C57: value 470p -> 100 pF
- C56: value 1uF -> 1 uF
- C58: value 1uF -> 18 pF
- C59: value 470p -> 0.1uF
- C60: value 1uF -> 0.1uF
- C69: value 300pF -> 470p
- C70: value 300pF -> 1uF
- C72: value 18 pF -> 300pF
- C79: value 100 pF -> 1 uF
- C81: value 100 pF -> 18 pF
- C82: value 1 uF -> 0.1uF
- C83, C89: value 100 pF -> 0.1uF
- C84: value 1 uF -> 100pF
- C85, C90: value 100 pF -> 100pF
- C86, C87, C88, C91, C94, C96: value 100 pF -> 300pF
- C92: value 100 pF -> 470p
- C93: value 1 uF -> 1uF
- C95: value 1 uF -> 300pF
- C97: value 1 uF -> 18 pF
- IC1, IC2, IC3: footprint GP2Y1+:QFN51P300X300X89-13N -> tx_board_footprints:QFN51P300X300X89-13N
- IC10, IC8: value MAPS-010164-TR0500 -> QPA9122TR7; footprint MAPS-010164-TR0500:QFN50P400X400X100-25N-D -> tx_board_footprints:QPA9122TR7
- IC11, IC13: value QPA9122TR7 -> MAPS-010164-TR0500; footprint QPA9122TR7:QPA9122TR7 -> tx_board_footprints:QFN50P400X400X100-25N-D
- IC12, IC14: footprint QPA9122TR7:QPA9122TR7 -> tx_board_footprints:QPA9122TR7
- IC4: footprint LT3041ADE:SON50P300X400X80-15N-D -> tx_board_footprints:SON50P300X400X80-15N-D
- IC5: footprint LT3099ADE:SON50P300X400X80-15N-D -> tx_board_footprints:SON50P300X400X80-15N-D
- IC6: footprint ADPL40502:SOT95P280X100-5N -> tx_board_footprints:SOT95P280X100-5N
- IC7, IC9: footprint MAPS-010164-TR0500:QFN50P400X400X100-25N-D -> tx_board_footprints:QFN50P400X400X100-25N-D
- J10, J11, J12, J13, J14, J16, J17, J19, J20, J9: footprint MM8030:MM80302610RJ3 -> tx_board_footprints:MM80302610RJ3
- J15, J18: value MM8030-2610RJ3 -> Conn_Coaxial; footprint MM8030:MM80302610RJ3 -> Connector_Coaxial:SMA_Amphenol_132289_EdgeMount
- J22, J23: value Conn_Coaxial -> MM8030-2610RJ3; footprint Connector_Coaxial:SMA_Amphenol_132289_EdgeMount -> tx_board_footprints:MM80302610RJ3
- R25, R37: value 10 -> 8.2
- R26, R28, R29, R38, R40, R41: value 10 -> 0
- R27, R39: value 10 -> 51
- R46, R47, R48: value 8.2 -> 10
- R51, R63: value 0 -> 51
- R54, R55, R56, R57: value 51 -> 10
- R58, R59, R60: value 0 -> 10
- R61: value 0 -> 8.2
- U1: footprint SN74HCT138NSR:NS16 -> tx_board_footprints:NS16
- moved J8 134.1 mm to (29.3, 34.8)
- moved J2 111.6 mm to (41.4, 44.7)
- moved J3 111.6 mm to (41.4, 48.8)
- moved J4 111.6 mm to (41.4, 52.8)
- moved J5 111.6 mm to (41.4, 56.9)
- moved R49 109.9 mm to (48.5, 80.7)
- moved R50 109.9 mm to (48.5, 82.7)
- moved J7 109.5 mm to (58.2, 50.7)
- moved R12 109.0 mm to (62.7, 35.4)
- moved R13 109.0 mm to (62.7, 37.1)
- moved R14 109.0 mm to (62.7, 38.9)
- moved R15 109.0 mm to (62.7, 40.6)
- moved R16 109.0 mm to (62.7, 42.4)
- moved R17 109.0 mm to (62.7, 44.1)
- moved R4 109.0 mm to (62.7, 33.6)
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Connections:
- C100 pad 1: Net-(C100-Pad1) -> GND
- C100 pad 2: GND -> Net-(C100-Pad2)
- C101 pad 1: Net-(C100-Pad1) -> Net-(C100-Pad2)
- C102 pad 1: Net-(IC12-RFOUT/VCC3_1) -> Net-(C102-Pad1)
- C102 pad 2: Net-(J22-In) -> GND
- C103 pad 1: Net-(IC13-RFOUT/VCC3_1) -> Net-(C102-Pad1)
- C103 pad 2: Net-(J23-In) -> GND
- C14 pad 1: VCC -> GND
- C14 pad 2: GND -> VEE
- C16 pad 1: VCC -> GND
- C16 pad 2: GND -> VEE
- C17 pad 1: GND -> Net-(IC7-D1_OR_SER_IN)
- C17 pad 2: VEE -> GND
- C18 pad 1: VCC -> GND
- C18 pad 2: GND -> Net-(IC7-D2_OR_CLK)
- C19 pad 2: VEE -> Net-(IC7-D3_OR_LE)
- C21 pad 2: VEE -> VCC
- C22 pad 1: VCC -> Net-(IC7-SER_OUT)
- C23 pad 1: GND -> VCC
- C23 pad 2: VEE -> GND
- C25 pad 1: GND -> Net-(AT1-SI)
- C25 pad 2: VEE -> GND
- C26 pad 1: GND -> Net-(AT1-CLK)
- C26 pad 2: VEE -> GND
- C27 pad 2: VEE -> Net-(AT1-LE)
- C28 pad 1: GND -> Net-(AT1-RFOUT)
- C28 pad 2: VEE -> Net-(J14-IN)
- C29 pad 1: Net-(IC7-D1_OR_SER_IN) -> VCC
- C30 pad 1: Net-(IC8-D1_OR_SER_IN) -> VCC
- C31 pad 1: Net-(IC9-D1_OR_SER_IN) -> GND
- C31 pad 2: GND -> Net-(C31-Pad2)
- C32 pad 1: Net-(IC10-D1_OR_SER_IN) -> Net-(C31-Pad2)
- C33 pad 1: GND -> Net-(C33-Pad1)
- C33 pad 2: Net-(IC7-D2_OR_CLK) -> GND
- C34 pad 1: GND -> Net-(C33-Pad1)
- C34 pad 2: Net-(IC8-D2_OR_CLK) -> GND
- C35 pad 1: GND -> Net-(IC8-RFOUT/VCC3_1)
- C35 pad 2: Net-(IC9-D2_OR_CLK) -> Net-(J15-In)
- C36 pad 1: GND -> VCC
- C36 pad 2: Net-(IC7-D3_OR_LE) -> GND
- C37 pad 2: Net-(IC10-D2_OR_CLK) -> VEE
- C38 pad 1: GND -> VCC
- C38 pad 2: Net-(IC8-D3_OR_LE) -> GND
- C39 pad 2: Net-(IC9-D3_OR_LE) -> VEE
- C40 pad 1: GND -> Net-(IC9-D1_OR_SER_IN)
- C40 pad 2: Net-(IC10-D3_OR_LE) -> GND
- C41 pad 1: VCC -> GND
- C41 pad 2: GND -> Net-(IC9-D2_OR_CLK)
- C42 pad 2: VCC -> Net-(IC9-D3_OR_LE)
- C45 pad 1: VCC -> Net-(IC9-SER_OUT)
- C46 pad 1: GND -> VCC
- C46 pad 2: VCC -> GND
- C48 pad 1: GND -> Net-(AT2-SI)
- C48 pad 2: VCC -> GND
- C49 pad 1: Net-(IC7-SER_OUT) -> Net-(AT2-CLK)
- C50 pad 1: Net-(IC8-SER_OUT) -> GND
- C50 pad 2: GND -> Net-(AT2-LE)
- C51 pad 1: Net-(IC9-SER_OUT) -> Net-(AT2-RFOUT)
- C51 pad 2: GND -> Net-(J17-IN)
- C52 pad 1: Net-(IC10-SER_OUT) -> VCC
- C54 pad 1: VCC -> GND
- C54 pad 2: GND -> Net-(C54-Pad2)
- C55 pad 1: VCC -> Net-(C54-Pad2)
- C56 pad 1: VCC -> Net-(C56-Pad1)
- C57 pad 1: VCC -> Net-(C56-Pad1)
- C58 pad 1: VCC -> Net-(IC10-RFOUT/VCC3_1)
- C58 pad 2: GND -> Net-(J18-In)
- C60 pad 1: VCC -> GND
- C60 pad 2: GND -> VEE
- C61 pad 1: Net-(AT1-SI) -> VCC
- C62 pad 1: Net-(AT2-SI) -> GND
- C62 pad 2: GND -> VEE
- C63 pad 1: Net-(AT3-SI) -> Net-(IC11-D1_OR_SER_IN)
- C64 pad 1: Net-(AT4-SI) -> GND
- C64 pad 2: GND -> Net-(IC11-D2_OR_CLK)
- C65 pad 1: Net-(AT1-CLK) -> GND
- C65 pad 2: GND -> Net-(IC11-D3_OR_LE)
- C66 pad 1: Net-(AT2-CLK) -> VCC
- C67 pad 1: Net-(AT3-CLK) -> GND
- C67 pad 2: GND -> VCC
- C68 pad 1: Net-(AT4-CLK) -> Net-(IC11-SER_OUT)
- C69 pad 1: GND -> VCC
- C69 pad 2: Net-(AT1-LE) -> GND
- C70 pad 1: GND -> VCC
- C70 pad 2: Net-(AT2-LE) -> GND
- C71 pad 1: GND -> Net-(AT3-SI)
- C71 pad 2: Net-(AT3-LE) -> GND
- C72 pad 1: Net-(AT1-RFOUT) -> Net-(AT3-CLK)
- C72 pad 2: Net-(J17-IN) -> GND
- C73 pad 2: Net-(AT4-LE) -> Net-(AT3-LE)
- C74 pad 1: Net-(AT2-RFOUT) -> Net-(AT3-RFOUT)
- C74 pad 2: Net-(J18-IN) -> Net-(J20-IN)
- C75 pad 1: Net-(AT3-RFOUT) -> VCC
- C75 pad 2: Net-(J19-IN) -> GND
- C76 pad 1: Net-(AT4-RFOUT) -> VCC
- C76 pad 2: Net-(J20-IN) -> GND
- C77 pad 1: VCC -> GND
- C77 pad 2: GND -> Net-(C77-Pad2)
- C78 pad 1: VCC -> Net-(C77-Pad2)
- C79 pad 1: VCC -> Net-(C79-Pad1)
- C80 pad 1: VCC -> Net-(C79-Pad1)
- C81 pad 1: VCC -> Net-(IC12-RFOUT/VCC3_1)
- C81 pad 2: GND -> Net-(J21-In)
- C83 pad 1: VCC -> GND
- C83 pad 2: GND -> VEE
- C85 pad 2: Net-(C85-Pad2) -> VEE
- C86 pad 1: GND -> Net-(IC13-D1_OR_SER_IN)
- C86 pad 2: Net-(C86-Pad2) -> GND
- C87 pad 2: Net-(C87-Pad2) -> Net-(IC13-D2_OR_CLK)
- C88 pad 2: Net-(C88-Pad2) -> Net-(IC13-D3_OR_LE)
- C89 pad 1: Net-(C85-Pad2) -> VCC
- C90 pad 1: Net-(C86-Pad2) -> GND
- C90 pad 2: GND -> VCC
- C91 pad 1: Net-(C87-Pad2) -> Net-(IC13-SER_OUT)
- C92 pad 1: Net-(C88-Pad2) -> VCC
- C93 pad 1: Net-(C93-Pad1) -> VCC
- C94 pad 1: Net-(C93-Pad1) -> Net-(AT4-SI)
- C95 pad 1: Net-(C95-Pad1) -> Net-(AT4-CLK)
- C96 pad 1: Net-(C95-Pad1) -> GND
- C96 pad 2: GND -> Net-(AT4-LE)
- C97 pad 1: Net-(C97-Pad1) -> Net-(AT4-RFOUT)
- C97 pad 2: GND -> Net-(J23-IN)
- C98 pad 1: Net-(C97-Pad1) -> VCC
- C99 pad 1: Net-(IC11-RFOUT/VCC3_1) -> VCC
- C99 pad 2: Net-(J21-In) -> GND
- IC10 pad 1: VEE -> GND
- IC10 pad 10: GND -> Net-(IC10-RFOUT/VCC3_1)
- IC10 pad 11: GND -> Net-(IC10-RFOUT/VCC3_1)
- IC10 pad 13: GND -> Net-(IC10-VBIAS)
- IC10 pad 14: Net-(IC10-RF_OUT) -> GND
- IC10 pad 16: GND -> Net-(IC10-VPD)
- IC10 pad 17: Net-(IC10-SER_OUT) -> GND
- IC10 pad 2: VCC -> Net-(IC10-RFIN)
- IC10 pad 4: GND -> Net-(IC10-VCC1/VCC2)
- IC10 pad 5: RF_IN1 -> GND
- IC11 pad 1: GND -> VEE
- IC11 pad 10: Net-(IC11-RFOUT/VCC3_1) -> GND
- IC11 pad 11: Net-(IC11-RFOUT/VCC3_1) -> GND
- IC11 pad 13: Net-(IC11-VBIAS) -> GND
- IC11 pad 14: GND -> Net-(IC11-RF_OUT)
- IC11 pad 16: Net-(IC11-VPD) -> GND
- IC11 pad 17: GND -> Net-(IC11-SER_OUT)
- IC11 pad 2: Net-(IC11-RFIN) -> VCC
- IC11 pad 4: Net-(IC11-VCC1/VCC2) -> GND
- IC11 pad 5: GND -> RF_IN3
- IC13 pad 1: GND -> VEE
- IC13 pad 10: Net-(IC13-RFOUT/VCC3_1) -> GND
- IC13 pad 11: Net-(IC13-RFOUT/VCC3_1) -> GND
- IC13 pad 13: Net-(IC13-VBIAS) -> GND
- IC13 pad 14: GND -> Net-(IC13-RF_OUT)
- IC13 pad 16: Net-(IC13-VPD) -> GND
- IC13 pad 17: GND -> Net-(IC13-SER_OUT)
- IC13 pad 2: Net-(IC13-RFIN) -> VCC
- IC13 pad 4: Net-(IC13-VCC1/VCC2) -> GND
- IC13 pad 5: GND -> RF_IN4
- IC7 pad 5: RF_IN4 -> RF_IN1
- IC8 pad 1: VEE -> GND
- IC8 pad 10: GND -> Net-(IC8-RFOUT/VCC3_1)
- IC8 pad 11: GND -> Net-(IC8-RFOUT/VCC3_1)
- IC8 pad 13: GND -> Net-(IC8-VBIAS)
- IC8 pad 14: Net-(IC8-RF_OUT) -> GND
- IC8 pad 16: GND -> Net-(IC8-VPD)
- IC8 pad 17: Net-(IC8-SER_OUT) -> GND
- IC8 pad 2: VCC -> Net-(IC8-RFIN)
- IC8 pad 4: GND -> Net-(IC8-VCC1/VCC2)
- IC8 pad 5: RF_IN2 -> GND
- IC9 pad 5: RF_IN3 -> RF_IN2
- J13 pad 1: Net-(IC8-RF_OUT) -> Net-(IC7-RF_OUT)
- J13 pad 2: Net-(AT2-RFIN) -> Net-(AT1-RFIN)
- J14 pad 1: Net-(IC9-RF_OUT) -> Net-(J14-IN)
- J14 pad 2: Net-(AT3-RFIN) -> Net-(IC8-RFIN)
- J15 pad 1: Net-(IC7-RF_OUT) -> Net-(J15-In)
- J15 pad 2: Net-(AT1-RFIN) -> GND
- J16 pad 1: Net-(IC10-RF_OUT) -> Net-(IC9-RF_OUT)
- J16 pad 2: Net-(AT4-RFIN) -> Net-(AT2-RFIN)
- J17 pad 2: Net-(IC11-RFIN) -> Net-(IC10-RFIN)
- J18 pad 1: Net-(J18-IN) -> Net-(J18-In)
- J18 pad 2: Net-(IC12-RFIN) -> GND
- J19 pad 1: Net-(J19-IN) -> Net-(IC11-RF_OUT)
- J19 pad 2: Net-(IC13-RFIN) -> Net-(AT3-RFIN)
- J20 pad 2: Net-(IC14-RFIN) -> Net-(IC12-RFIN)
- J22 pad 1: Net-(J22-In) -> Net-(IC13-RF_OUT)
- J22 pad 2: GND -> Net-(AT4-RFIN)
- J23 pad 1: Net-(J23-In) -> Net-(J23-IN)
- J23 pad 2: GND -> Net-(IC14-RFIN)
- L1 pad 1: Net-(IC11-RFOUT/VCC3_1) -> Net-(IC8-RFOUT/VCC3_1)
- L1 pad 2: Net-(C93-Pad1) -> Net-(C33-Pad1)
- L2 pad 1: Net-(IC12-RFOUT/VCC3_1) -> Net-(IC10-RFOUT/VCC3_1)
- L2 pad 2: Net-(C95-Pad1) -> Net-(C56-Pad1)
- L3 pad 1: Net-(IC13-RFOUT/VCC3_1) -> Net-(IC12-RFOUT/VCC3_1)
- L3 pad 2: Net-(C97-Pad1) -> Net-(C79-Pad1)
- L4 pad 2: Net-(C100-Pad1) -> Net-(C102-Pad1)
- R19 pad 1: PS_SER_IN -> PS_CLK
- R19 pad 2: Net-(IC8-D1_OR_SER_IN) -> Net-(IC7-D2_OR_CLK)
- R20 pad 1: PS_SER_IN -> Net-(IC7-D3_OR_LE)
- R20 pad 2: Net-(IC9-D1_OR_SER_IN) -> PS_LE_1
- R21 pad 1: PS_SER_IN -> PS_SER_OUT
- R21 pad 2: Net-(IC10-D1_OR_SER_IN) -> Net-(IC7-SER_OUT)
- R22 pad 1: PS_CLK -> ATTN_SI
- R22 pad 2: Net-(IC7-D2_OR_CLK) -> Net-(AT1-SI)
- R23 pad 1: PS_CLK -> Net-(AT1-CLK)
- R23 pad 2: Net-(IC8-D2_OR_CLK) -> ATTN_CLK
- R24 pad 1: PS_CLK -> Net-(AT1-LE)
- R24 pad 2: Net-(IC9-D2_OR_CLK) -> ATTN_LE_1
- R25 pad 1: Net-(IC7-D3_OR_LE) -> VCC
- R25 pad 2: PS_LE_4 -> Net-(IC8-VCC1/VCC2)
- R26 pad 1: PS_CLK -> V_PD
- R26 pad 2: Net-(IC10-D2_OR_CLK) -> Net-(IC8-VPD)
- R27 pad 1: Net-(IC8-D3_OR_LE) -> Net-(C31-Pad2)
- R27 pad 2: PS_LE_2 -> Net-(IC8-VBIAS)
- R28 pad 1: Net-(IC9-D3_OR_LE) -> Net-(C31-Pad2)
- R28 pad 2: PS_LE_3 -> VCC
- R29 pad 1: Net-(IC10-D3_OR_LE) -> Net-(C33-Pad1)
- R29 pad 2: PS_LE_1 -> VCC
- R30 pad 1: PS_SER_OUT -> PS_SER_IN
- R30 pad 2: Net-(IC7-SER_OUT) -> Net-(IC9-D1_OR_SER_IN)
- R31 pad 1: PS_SER_OUT -> PS_CLK
- R31 pad 2: Net-(IC8-SER_OUT) -> Net-(IC9-D2_OR_CLK)
- R32 pad 1: PS_SER_OUT -> Net-(IC9-D3_OR_LE)
- R32 pad 2: Net-(IC9-SER_OUT) -> PS_LE_1
- R33 pad 2: Net-(IC10-SER_OUT) -> Net-(IC9-SER_OUT)
- R34 pad 2: Net-(AT1-SI) -> Net-(AT2-SI)
- R35 pad 1: ATTN_SI -> Net-(AT2-CLK)
- R35 pad 2: Net-(AT2-SI) -> ATTN_CLK
- R36 pad 1: ATTN_SI -> Net-(AT2-LE)
- R36 pad 2: Net-(AT3-SI) -> ATTN_LE_1
- R37 pad 1: ATTN_SI -> VCC
- R37 pad 2: Net-(AT4-SI) -> Net-(IC10-VCC1/VCC2)
- R38 pad 1: Net-(AT1-CLK) -> V_PD
- R38 pad 2: ATTN_CLK -> Net-(IC10-VPD)
- R39 pad 1: Net-(AT2-CLK) -> Net-(C54-Pad2)
- R39 pad 2: ATTN_CLK -> Net-(IC10-VBIAS)
- R40 pad 1: Net-(AT3-CLK) -> Net-(C54-Pad2)
- R40 pad 2: ATTN_CLK -> VCC
- R41 pad 1: Net-(AT4-CLK) -> Net-(C56-Pad1)
- R41 pad 2: ATTN_CLK -> VCC
- R42 pad 1: Net-(AT1-LE) -> PS_SER_IN
- R42 pad 2: ATTN_LE_4 -> Net-(IC11-D1_OR_SER_IN)
- R43 pad 1: Net-(AT2-LE) -> PS_CLK
- R43 pad 2: ATTN_LE_2 -> Net-(IC11-D2_OR_CLK)
- R44 pad 1: Net-(AT3-LE) -> Net-(IC11-D3_OR_LE)
- R44 pad 2: ATTN_LE_3 -> PS_LE_1
- R45 pad 1: Net-(AT4-LE) -> PS_SER_OUT
- R45 pad 2: ATTN_LE_1 -> Net-(IC11-SER_OUT)
- R46 pad 1: VCC -> ATTN_SI
- R46 pad 2: Net-(IC11-VCC1/VCC2) -> Net-(AT3-SI)
- R47 pad 1: VCC -> Net-(AT3-CLK)
- R47 pad 2: Net-(IC12-VCC1/VCC2) -> ATTN_CLK
- R48 pad 1: VCC -> Net-(AT3-LE)
- R48 pad 2: Net-(IC13-VCC1/VCC2) -> ATTN_LE_1
- R49 pad 2: Net-(IC14-VCC1/VCC2) -> Net-(IC12-VCC1/VCC2)
- R50 pad 2: Net-(IC11-VPD) -> Net-(IC12-VPD)
- R51 pad 1: V_PD -> Net-(C77-Pad2)
- R51 pad 2: Net-(IC12-VPD) -> Net-(IC12-VBIAS)
- R52 pad 1: V_PD -> Net-(C77-Pad2)
- R52 pad 2: Net-(IC13-VPD) -> VCC
- R53 pad 1: V_PD -> Net-(C79-Pad1)
- R53 pad 2: Net-(IC14-VPD) -> VCC
- R54 pad 1: Net-(C85-Pad2) -> PS_SER_IN
- R54 pad 2: Net-(IC11-VBIAS) -> Net-(IC13-D1_OR_SER_IN)
- R55 pad 1: Net-(C86-Pad2) -> PS_CLK
- R55 pad 2: Net-(IC12-VBIAS) -> Net-(IC13-D2_OR_CLK)
- R56 pad 1: Net-(C87-Pad2) -> Net-(IC13-D3_OR_LE)
- R56 pad 2: Net-(IC13-VBIAS) -> PS_LE_1
- R57 pad 1: Net-(C88-Pad2) -> PS_SER_OUT
- R57 pad 2: Net-(IC14-VBIAS) -> Net-(IC13-SER_OUT)
- R58 pad 1: Net-(C85-Pad2) -> ATTN_SI
- R58 pad 2: VCC -> Net-(AT4-SI)
- R59 pad 1: Net-(C86-Pad2) -> Net-(AT4-CLK)
- R59 pad 2: VCC -> ATTN_CLK
- R60 pad 1: Net-(C87-Pad2) -> Net-(AT4-LE)
- R60 pad 2: VCC -> ATTN_LE_1
- R61 pad 1: Net-(C88-Pad2) -> VCC
- R61 pad 2: VCC -> Net-(IC14-VCC1/VCC2)
- R62 pad 1: Net-(C93-Pad1) -> V_PD
- R62 pad 2: VCC -> Net-(IC14-VPD)
- R63 pad 1: Net-(C95-Pad1) -> Net-(C100-Pad2)
- R63 pad 2: VCC -> Net-(IC14-VBIAS)
- R64 pad 1: Net-(C97-Pad1) -> Net-(C100-Pad2)
- R65 pad 1: Net-(C100-Pad1) -> Net-(C102-Pad1)
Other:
- board outline removed
